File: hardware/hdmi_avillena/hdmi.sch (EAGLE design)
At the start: 5 parts

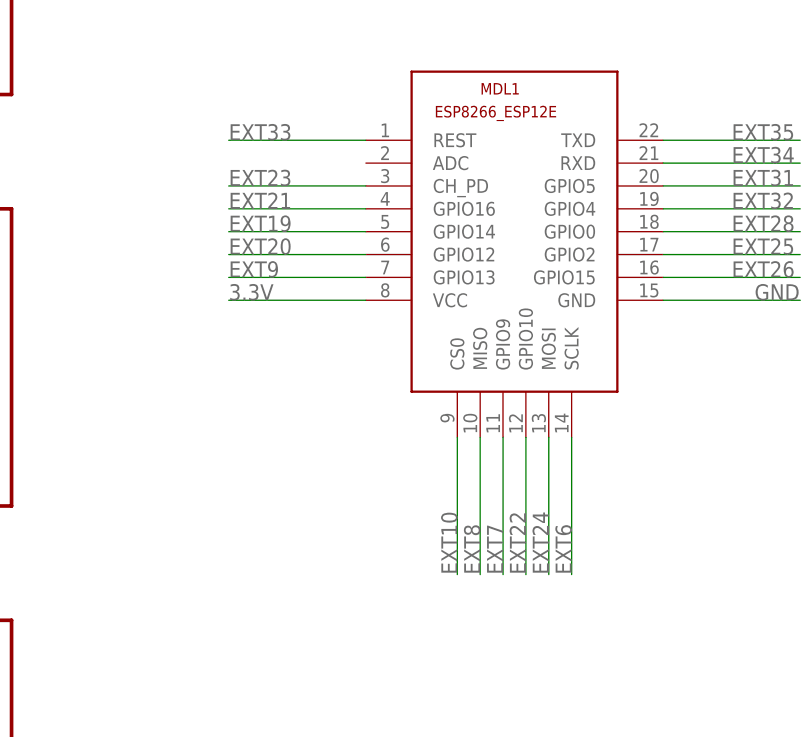
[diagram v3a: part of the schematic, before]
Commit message: Pongo conector HDMI y ESP12 por abajo para que abulte menos
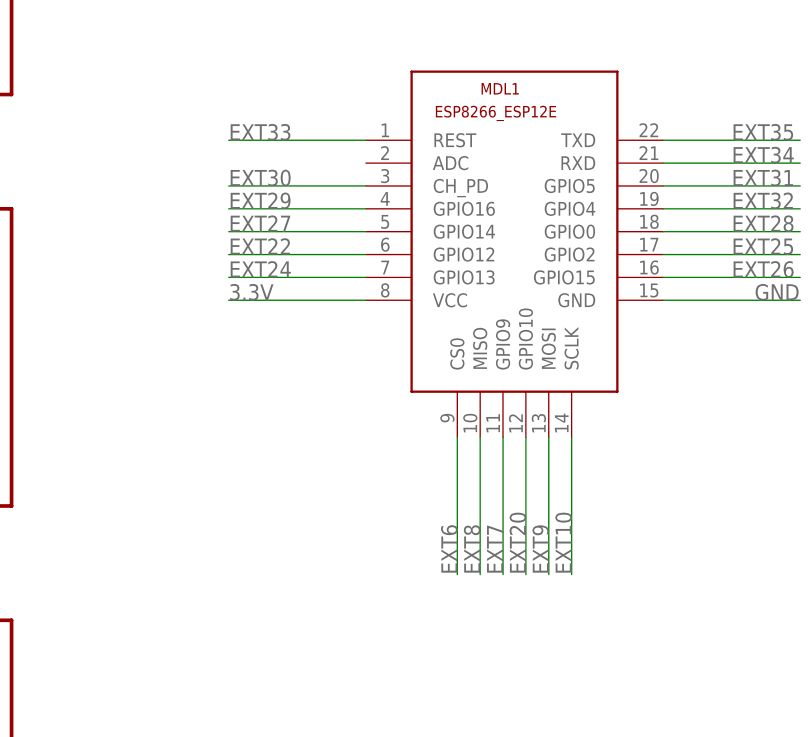
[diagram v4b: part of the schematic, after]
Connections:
- net EXT10: now also MDL1.SCLK; no longer MDL1.CS0
- net EXT19: no longer MDL1.GPIO14
- net EXT20: now also MDL1.GPIO10; no longer MDL1.GPIO12
- net EXT21: no longer MDL1.GPIO16
- net EXT22: now also MDL1.GPIO12; no longer MDL1.GPIO10
- net EXT23: no longer MDL1.CH_PD
- net EXT24: now also MDL1.GPIO13; no longer MDL1.MOSI
- net EXT27: now also MDL1.GPIO14
- net EXT29: now also MDL1.GPIO16
- net EXT30: now also MDL1.CH_PD
- net EXT6: now also MDL1.CS0; no longer MDL1.SCLK
- net EXT9: now also MDL1.MOSI; no longer MDL1.GPIO13

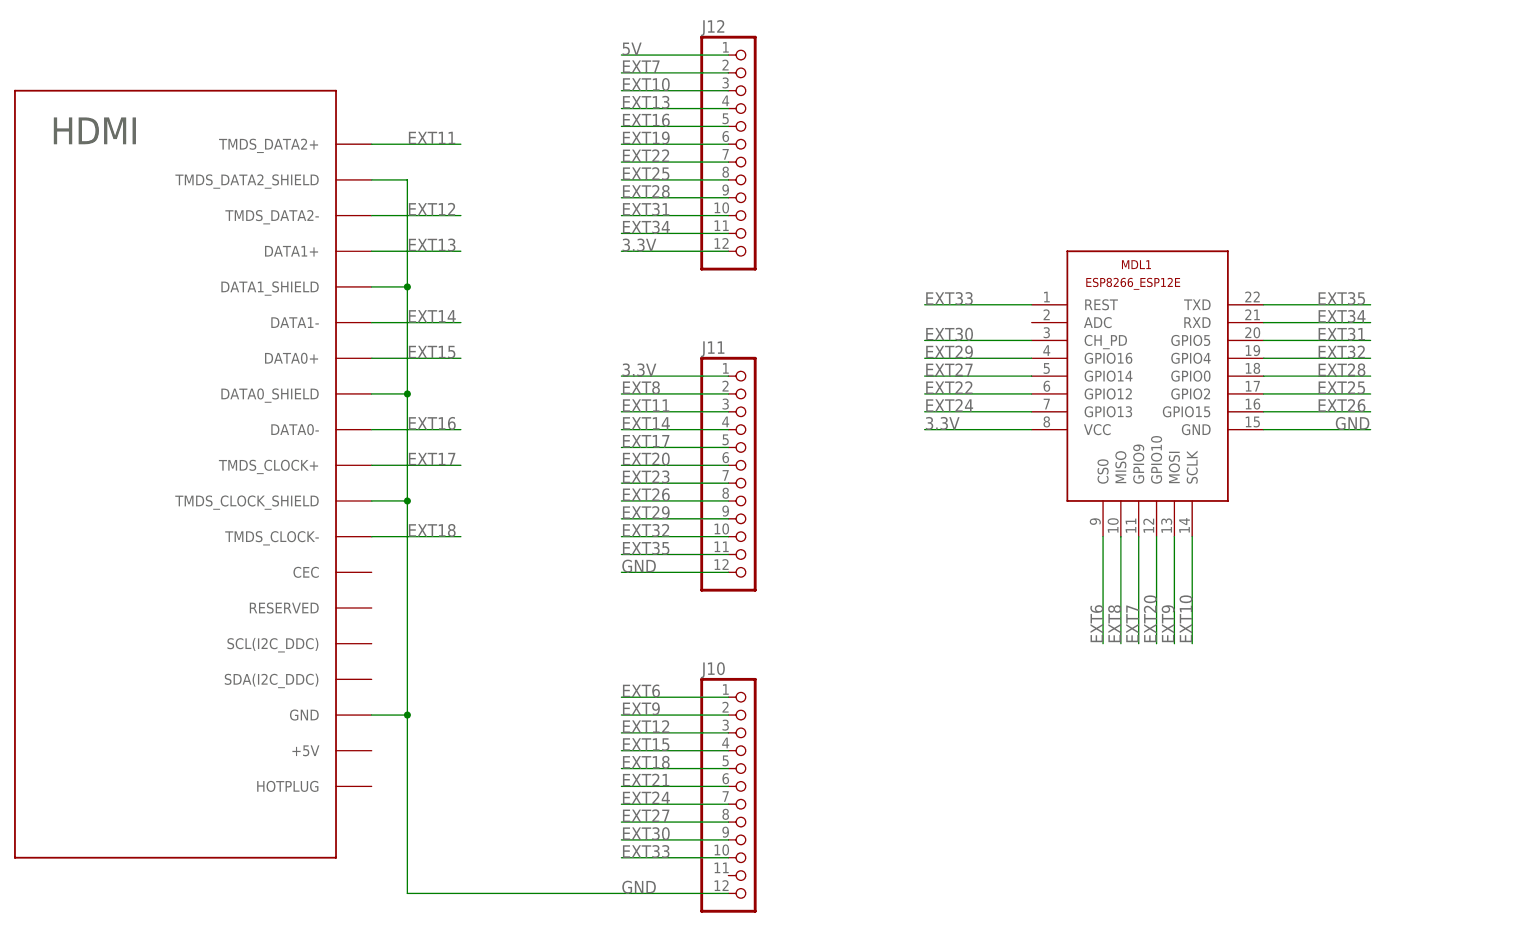
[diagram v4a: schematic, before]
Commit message: Añado esquema de yombo y aprovecho para cambiar huella de HDMI
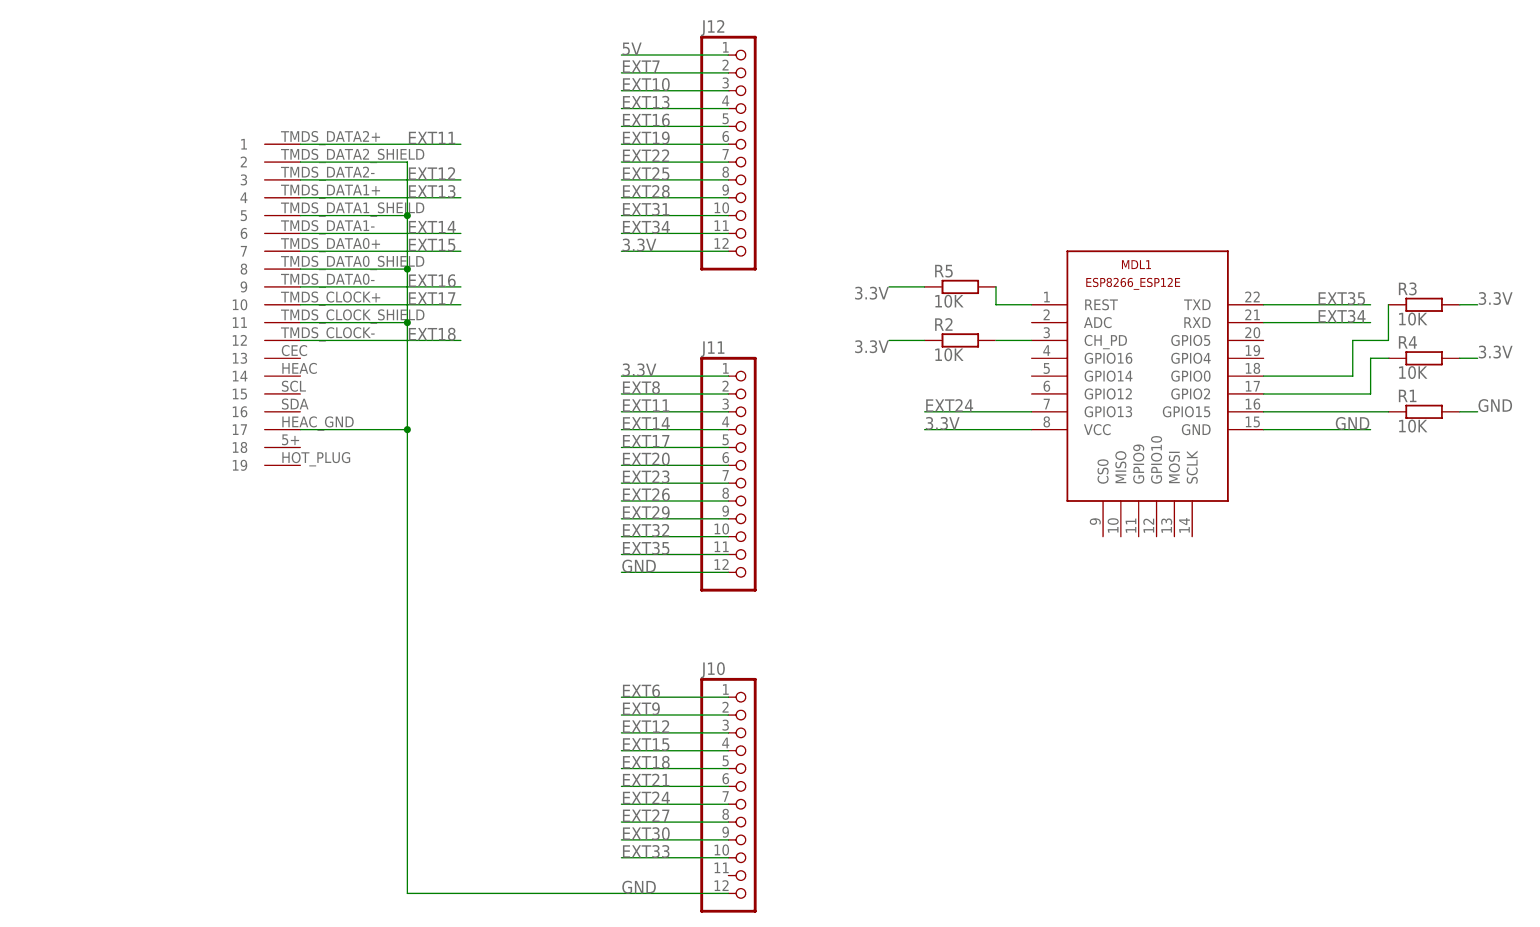
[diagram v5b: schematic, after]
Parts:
- removed U$1: HDMI, 00_cody:HDMI
- added R1, R2, R3, R4, R5: 10K, resistor-shunt:SMK
- added U$2: HDMI, Connfly:HDMI
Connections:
- new net N$1: MDL1.CH_PD, R2.1
- new net N$2: MDL1.GPIO15, R1.2
- new net N$3: MDL1.GPIO2, R4.2
- new net N$4: MDL1.GPIO0, R3.2
- new net N$5: MDL1.REST, R5.1
- net 3.3V: now also R2.2, R3.1, R4.1, R5.2
- net EXT10: no longer MDL1.SCLK
- net EXT11: now also U$2.1; no longer U$1.TMDS_DATA2+
- net EXT12: now also U$2.3; no longer U$1.TMDS_DATA2-
- net EXT13: now also U$2.4; no longer U$1.DATA1+
- net EXT14: now also U$2.6; no longer U$1.DATA1-
- net EXT15: now also U$2.7; no longer U$1.DATA0+
- net EXT16: now also U$2.9; no longer U$1.DATA0-
- net EXT17: now also U$2.10; no longer U$1.TMDS_CLOCK+
- net EXT18: now also U$2.12; no longer U$1.TMDS_CLOCK-
- net EXT20: no longer MDL1.GPIO10
- net EXT22: no longer MDL1.GPIO12
- net EXT25: no longer MDL1.GPIO2
- net EXT26: no longer MDL1.GPIO15
- net EXT27: no longer MDL1.GPIO14
- net EXT28: no longer MDL1.GPIO0
- net EXT29: no longer MDL1.GPIO16
- net EXT30: no longer MDL1.CH_PD
- net EXT31: no longer MDL1.GPIO5
- net EXT32: no longer MDL1.GPIO4
- net EXT33: no longer MDL1.REST
- net EXT6: no longer MDL1.CS0
- net EXT7: no longer MDL1.GPIO9
- net EXT8: no longer MDL1.MISO
- net EXT9: no longer MDL1.MOSI
- net GND: now also R1.1, U$2.11, U$2.17, U$2.2, U$2.5, U$2.8; no longer U$1.DATA0_SHIELD, U$1.DATA1_SHIELD, U$1.GND, U$1.TMDS_CLOCK_SHIELD, U$1.TMDS_DATA2_SHIELD

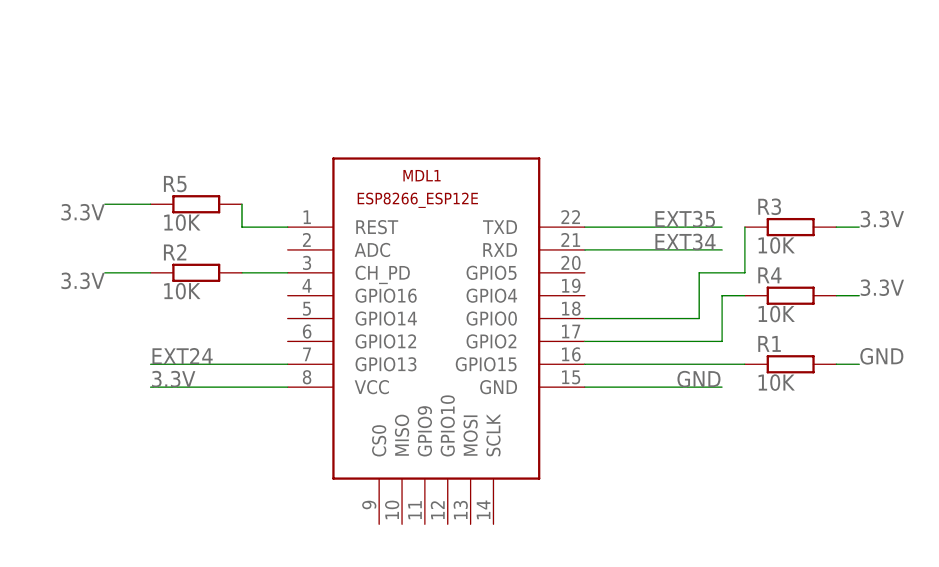
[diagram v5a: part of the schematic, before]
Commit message: Termino ruteado del addon HDMI
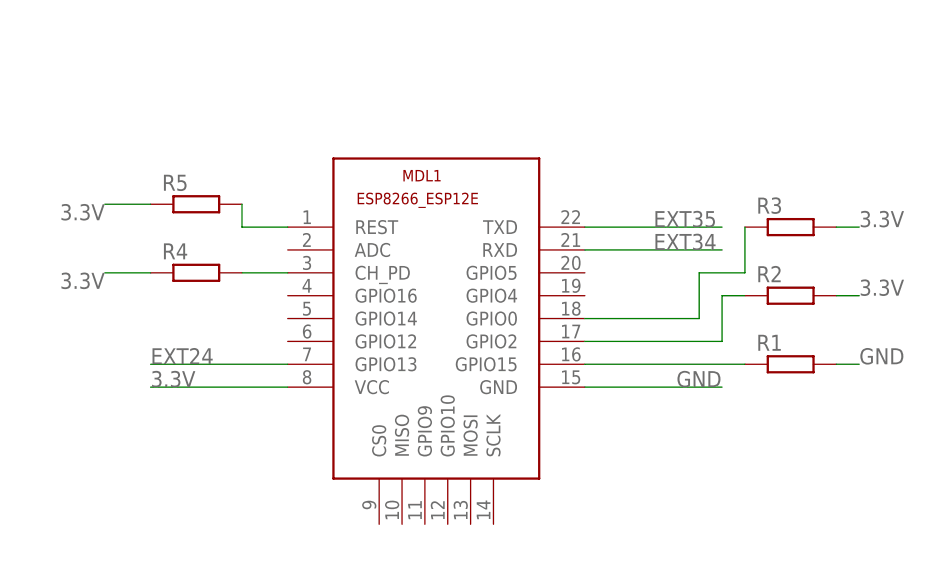
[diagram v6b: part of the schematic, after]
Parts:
- R1, R2, R3, R4, R5: value 10K -> (none); device resistor-shunt:SMK -> rcl:R-EU_M0805
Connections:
- net 3.3V: now also R3.2, R5.1; no longer R3.1, R5.2
- net GND: now also R1.2; no longer R1.1
- net N$1: now also R4.2; no longer R2.1
- net N$2: now also R1.1; no longer R1.2
- net N$3: now also R2.1; no longer R4.2
- net N$4: now also R3.1; no longer R3.2
- net N$5: now also R5.2; no longer R5.1
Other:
- moved on the sheet: R2, R4

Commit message: Últimas correcciones de yombo
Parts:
- removed R2, R3, R4, R5: (no value), rcl:R-EU_M0805
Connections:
- removed net N$2: MDL1.GPIO15, R1.1
- removed net N$3: MDL1.GPIO2, R2.1
- removed net N$4: MDL1.GPIO0, R3.1
- removed net N$5: MDL1.REST, R5.2
- net 3.3V: no longer R2.2, R3.2, R4.1, R5.1
- net EXT25: now also MDL1.GPIO2
- net EXT28: now also MDL1.GPIO0
- net EXT30: now also MDL1.CH_PD
- net EXT33: now also MDL1.REST
- net N$1: now also MDL1.GPIO4, R1.1; no longer MDL1.CH_PD, R4.2
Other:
- moved on the sheet: R1

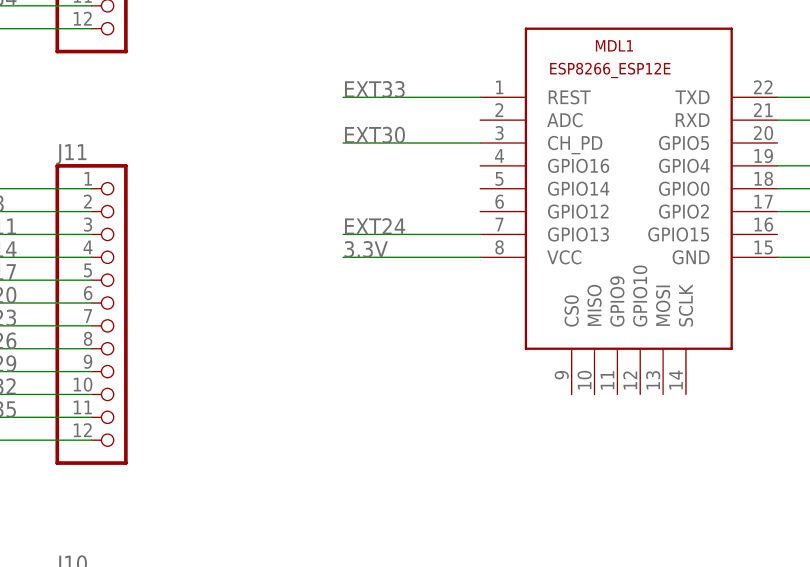
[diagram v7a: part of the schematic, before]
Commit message: Pongo jumper para desactivar alimentación del ESP12E
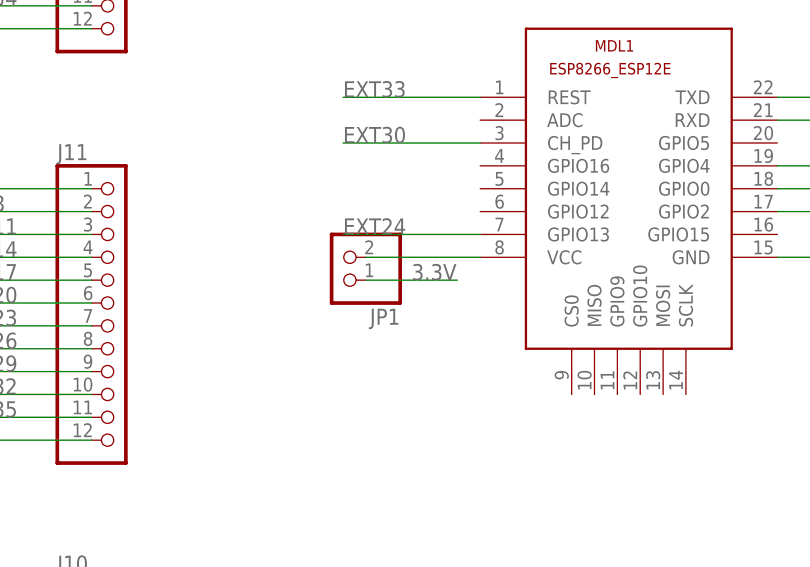
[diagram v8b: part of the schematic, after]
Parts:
- added JP1: (no value), pinhead:PINHD-1X2/90
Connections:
- new net N$2: JP1.2, MDL1.VCC
- net 3.3V: now also JP1.1; no longer MDL1.VCC
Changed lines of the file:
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@@
 <part name="U$2" library="Connfly" deviceset="HDMI" device=""/>
 <part name="R1" library="rcl" deviceset="R-EU_" device="M0805"/>
+<part name="JP1" library="pinhead" deviceset="PINHD-1X2" device="/90"/>
 </parts>
 <sheets>
@@
 <instance part="U$2" gate="G$1" x="-35.56" y="88.9" rot="MR270"/>
 <instance part="R1" gate="G$1" x="119.38" y="58.42"/>
+<instance part="JP1" gate="G$1" x="53.34" y="48.26" rot="R180"/>
 </instances>
 <busses>
@@
 </segment>
 <segment>
-<wire x1="68.58" y1="48.26" x2="53.34" y2="48.26" width="0.1524" layer="91"/>
-<label x="53.34" y="48.26" size="1.778" layer="95"/>
-<pinref part="MDL1" gate="G$1" pin="VCC"/>
+<pinref part="JP1" gate="G$1" pin="1"/>
+<wire x1="55.88" y1="45.72" x2="66.04" y2="45.72" width="0.1524" layer="91"/>
+<label x="60.96" y="45.72" size="1.778" layer="95"/>
 </segment>
 </net>
@@
 </segment>
 </net>
+<net name="N$2" class="0">
+<segment>
+<pinref part="JP1" gate="G$1" pin="2"/>
+<pinref part="MDL1" gate="G$1" pin="VCC"/>
+<wire x1="55.88" y1="48.26" x2="68.58" y2="48.26" width="0.1524" layer="91"/>
+</segment>
+</net>
